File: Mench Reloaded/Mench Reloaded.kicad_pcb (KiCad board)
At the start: 2 copper layers, 100 x 100 mm, 60 parts, among them IC1 DS1813, J1 XBUS_265, J10 FTDI serial, J11 Power Sel, J12 Int Sel, J13 VIA1 Port A, J14 VIA1 Port B, J2 TGx, J3 RAM CSB select, J4 P4x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

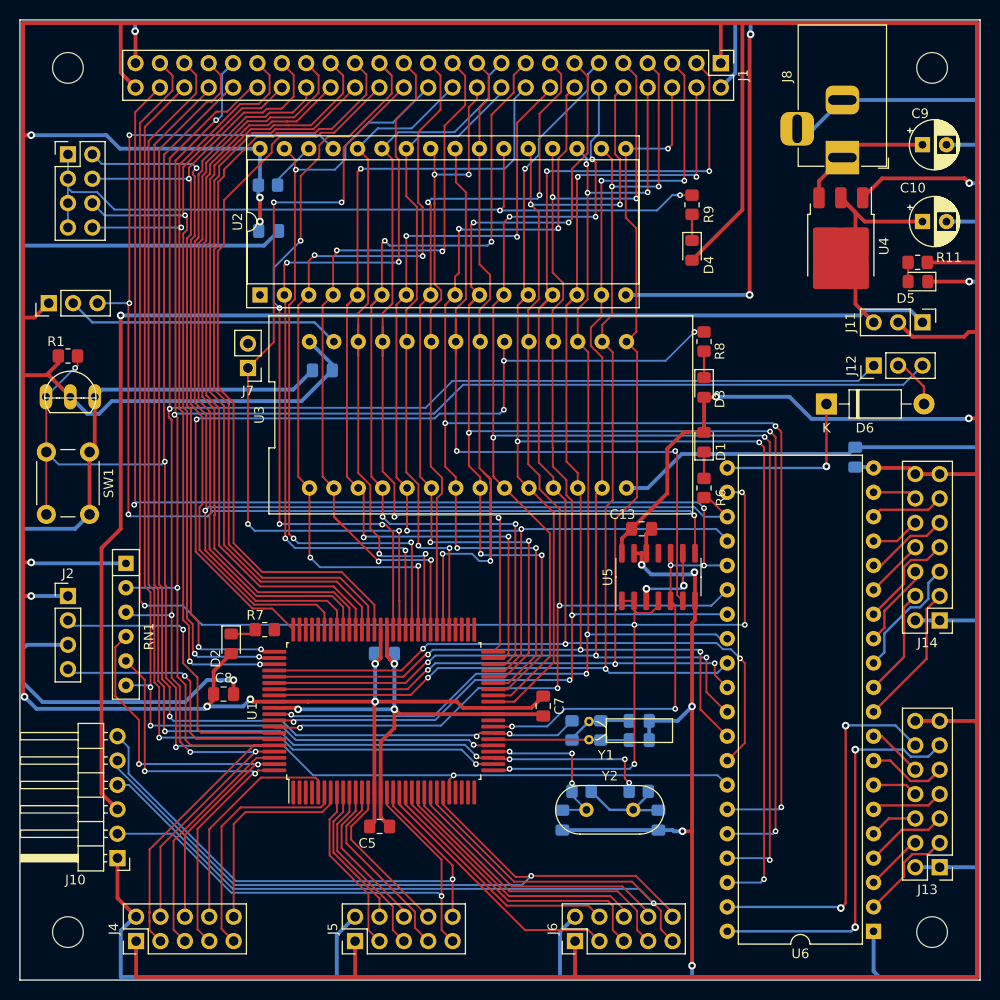
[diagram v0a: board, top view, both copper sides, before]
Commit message: Shifted blue traces north to allow moving decoupling cap to front side of board.
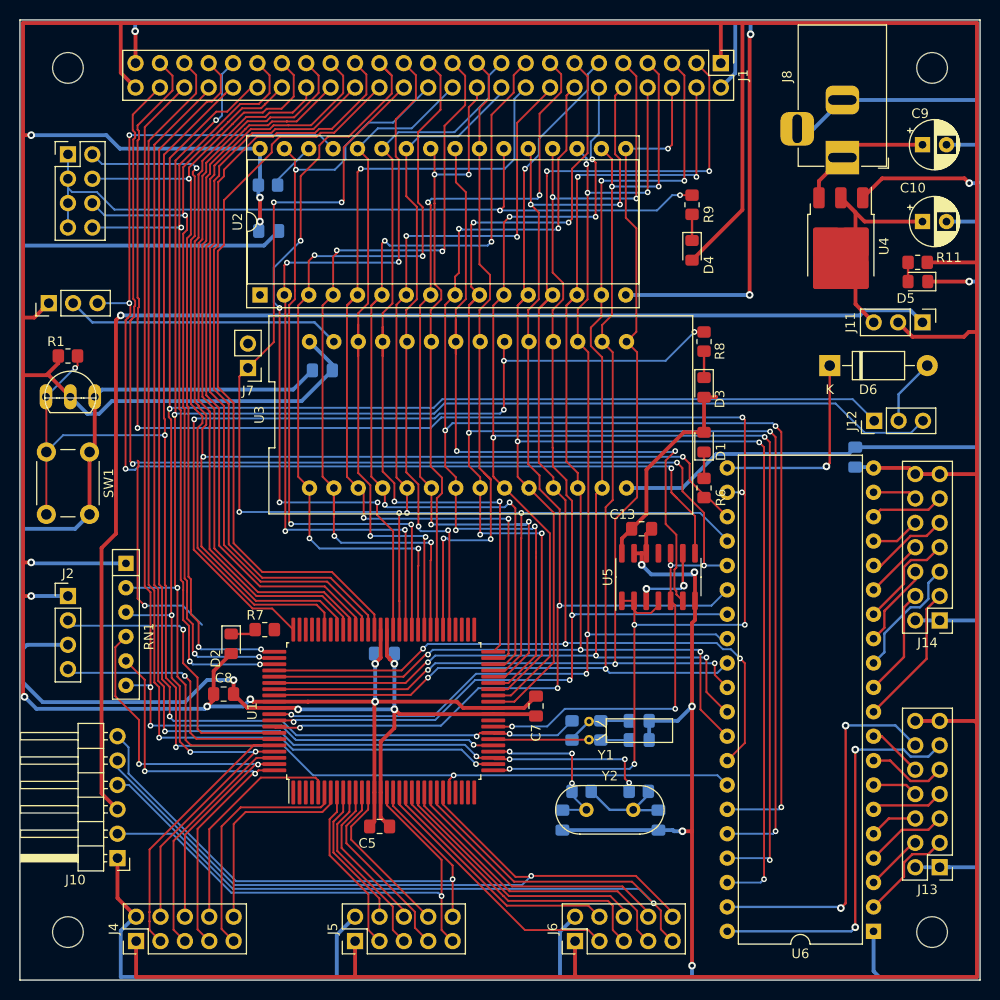
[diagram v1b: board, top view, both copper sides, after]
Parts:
- moved J12 5.75 mm to (144.0, 86.8)
- moved D6 4.01 mm to (139.3, 81.0)
- moved C7 0.75 mm to (108.8, 116.5)
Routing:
- net +5V: track 671.5 -> 643.2 mm, vias 12 -> 10
- net WEB: track 174.1 -> 197.9 mm, vias 6 -> 8
- net a10: track 77.1 -> 67.7 mm
- net Net-(D6-K): track 16.9 -> 21.0 mm
- net GND: track 766.5 -> 770.6 mm
- net a12: track 81.6 -> 85.5 mm
- net Net-(D6-A): track 5.41 -> 6.99 mm
- net a17: track 82.8 -> 84.3 mm
- net a4: track 90.3 -> 91.6 mm
- net MEMOEB: track 74.7 -> 75.7 mm
- net a16: track 84.1 -> 85.0 mm
- net a3: track 165.4 -> 166.3 mm
- net IRQB: track 185.5 -> 184.7 mm
- net csb0: track 78.3 -> 77.6 mm
- net PHI2: track 152.3 -> 151.6 mm
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
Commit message: All SMD components are now on the front side for hot plate assembly. Power rails are insent from edge and increased in size to 1mm.
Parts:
- C1, C11, C12, C14, C2, C3, C4, C6, R10, R2, R3, R4, R5: moved to F.Cu
- moved R10 21.7 mm to (60.0, 56.0)
- moved C4 14.2 mm to (107.5, 130.8)
- moved R4 12.0 mm to (107.5, 126.8), turned to 90 degrees
- moved C2 10.3 mm to (121.5, 130.8)
- moved C12 8.48 mm to (79.5, 86.3), turned to 90 degrees
- moved C6 5.75 mm to (93.0, 105.2)
- moved C14 5.37 mm to (137.8, 87.2), turned to 180 degrees
- moved C11 5.12 mm to (77.0, 70.2), turned to -90 degrees
- moved C3 4.75 mm to (119.5, 122.8), turned to -90 degrees
- moved C1 3.52 mm to (117.2, 122.7), turned to -90 degrees
- moved Y2 3.35 mm to (117.0, 128.8), turned to 180 degrees
- moved R2 3.00 mm to (112.5, 119.0)
- moved R5 2.85 mm to (113.2, 116.2), turned to 180 degrees
- moved C8 1.44 mm to (77.2, 116.2), turned to -90 degrees
- moved R3 1.30 mm to (112.2, 125.0), turned to 0 degrees
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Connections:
- U2 pad 1: unconnected-(U2-NC-Pad1) -> a17_Select
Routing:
- net +5V: track 643.2 -> 671.4 mm
- net MEMCS2: track 5.15 -> 25.1 mm, vias 0 -> 1
- net WEB: track 197.9 -> 180.0 mm, vias 8 -> 7
- net FCLKOB: track 122.2 -> 111.0 mm, vias 5 -> 2
- net GND: track 770.6 -> 760.6 mm
- net csb2: track 0.00 -> 7.89 mm
- net a17_Select: track 0.00 -> 4.73 mm
- net Net-(C4-Pad1): track 10.4 -> 14.2 mm
- net Net-(U1-FCLK): track 17.3 -> 20.7 mm, vias 3 -> 0
- net Net-(C3-Pad1): track 6.88 -> 10.3 mm
- net PHI2: track 151.6 -> 155.0 mm
- net a12: track 85.5 -> 82.5 mm
- net MEMWEB: track 127.9 -> 130.1 mm
- net d5: track 122.5 -> 123.8 mm
- net a18: track 78.7 -> 79.8 mm
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
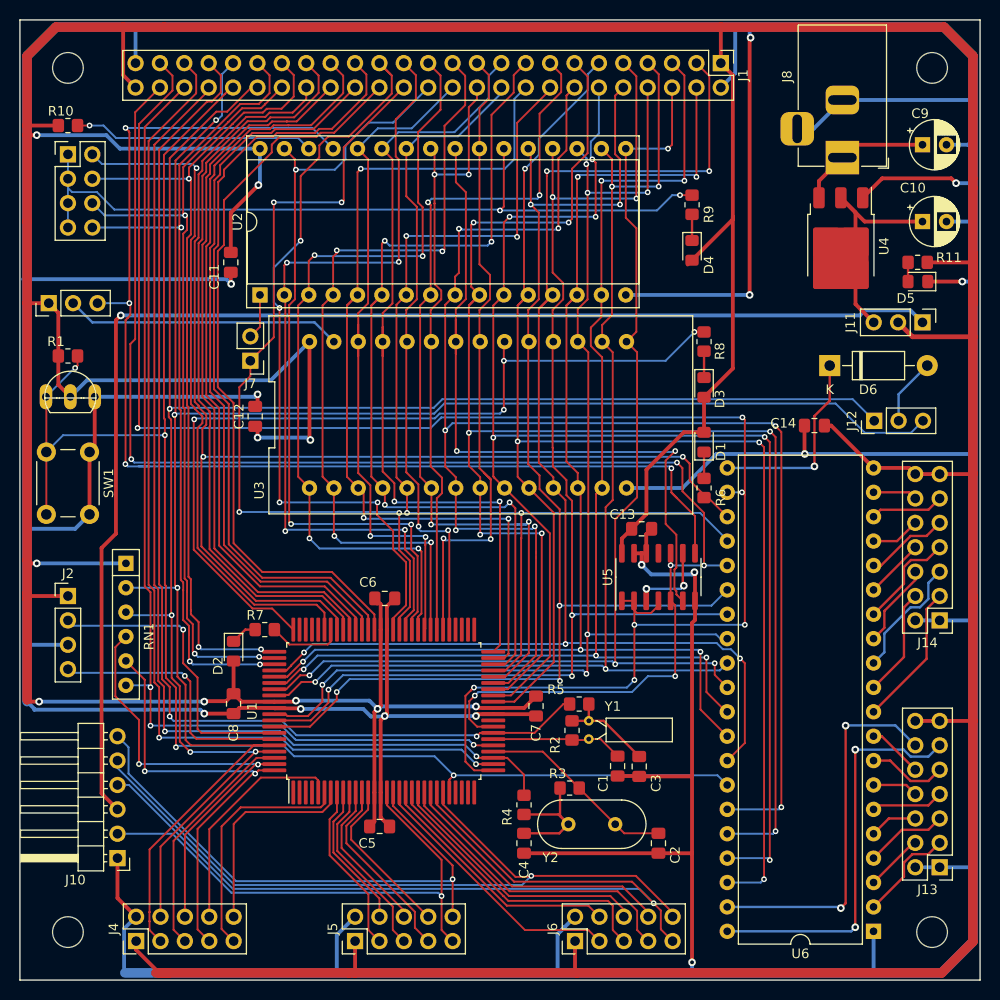
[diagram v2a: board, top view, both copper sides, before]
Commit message: Minor changes to quiet the ERC and DRC reports.
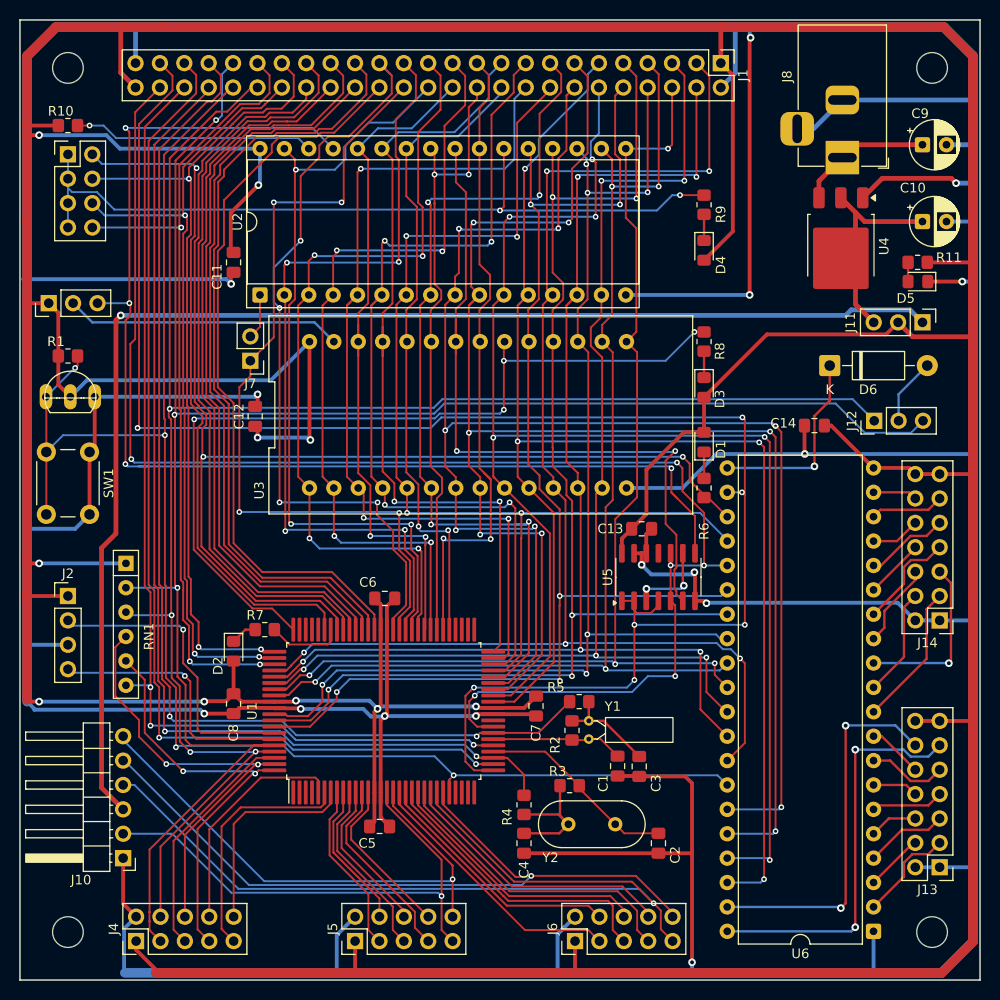
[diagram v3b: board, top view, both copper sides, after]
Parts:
- moved D4 1.25 mm to (126.2, 69.0)
- moved R9 1.25 mm to (126.2, 64.2)
- moved J10 0.59 mm to (65.8, 132.3)
- moved C11 0.29 mm to (77.2, 70.2)
- moved R3 0.25 mm to (112.2, 124.8)
- moved R5 0.25 mm to (113.2, 116.0)
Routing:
- net Net-(J14-Pin_5): track 12.9 -> 18.0 mm, vias 0 -> 1
- net GND: track 760.6 -> 764.3 mm, vias 14 -> 15
- net Net-(J11-Pin_3): track 23.3 -> 20.6 mm
- net d0: track 144.0 -> 141.6 mm
- net AMS: track 46.6 -> 44.3 mm
- net DSRB3: track 58.4 -> 56.4 mm
- net +5V: track 671.4 -> 673.1 mm
- net FA15: track 48.1 -> 46.4 mm
- net MEMCS1B: track 80.9 -> 82.1 mm
- net TXD3: track 79.6 -> 78.6 mm
- net RXD3: track 93.8 -> 94.4 mm
- net DTRB3: track 54.8 -> 54.2 mm

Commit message: Updated PCB after schematic changes for ERC. The results were just changes to description fields.
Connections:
- U1 pad 39: BA -> unconnected-(U1-BA/~{DOD}-Pad39)
